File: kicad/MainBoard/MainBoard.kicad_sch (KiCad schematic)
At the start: 97 parts, among them J1 CHAN1, J10 ACC Port, J11 433TX, J12 VDC INPUT, J13 BAT, J14 TRG1, J15 TRG2, J16 FP-BUTTONS, J17 EXPAN2, J18 OUTPUT_BOARD_POWER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

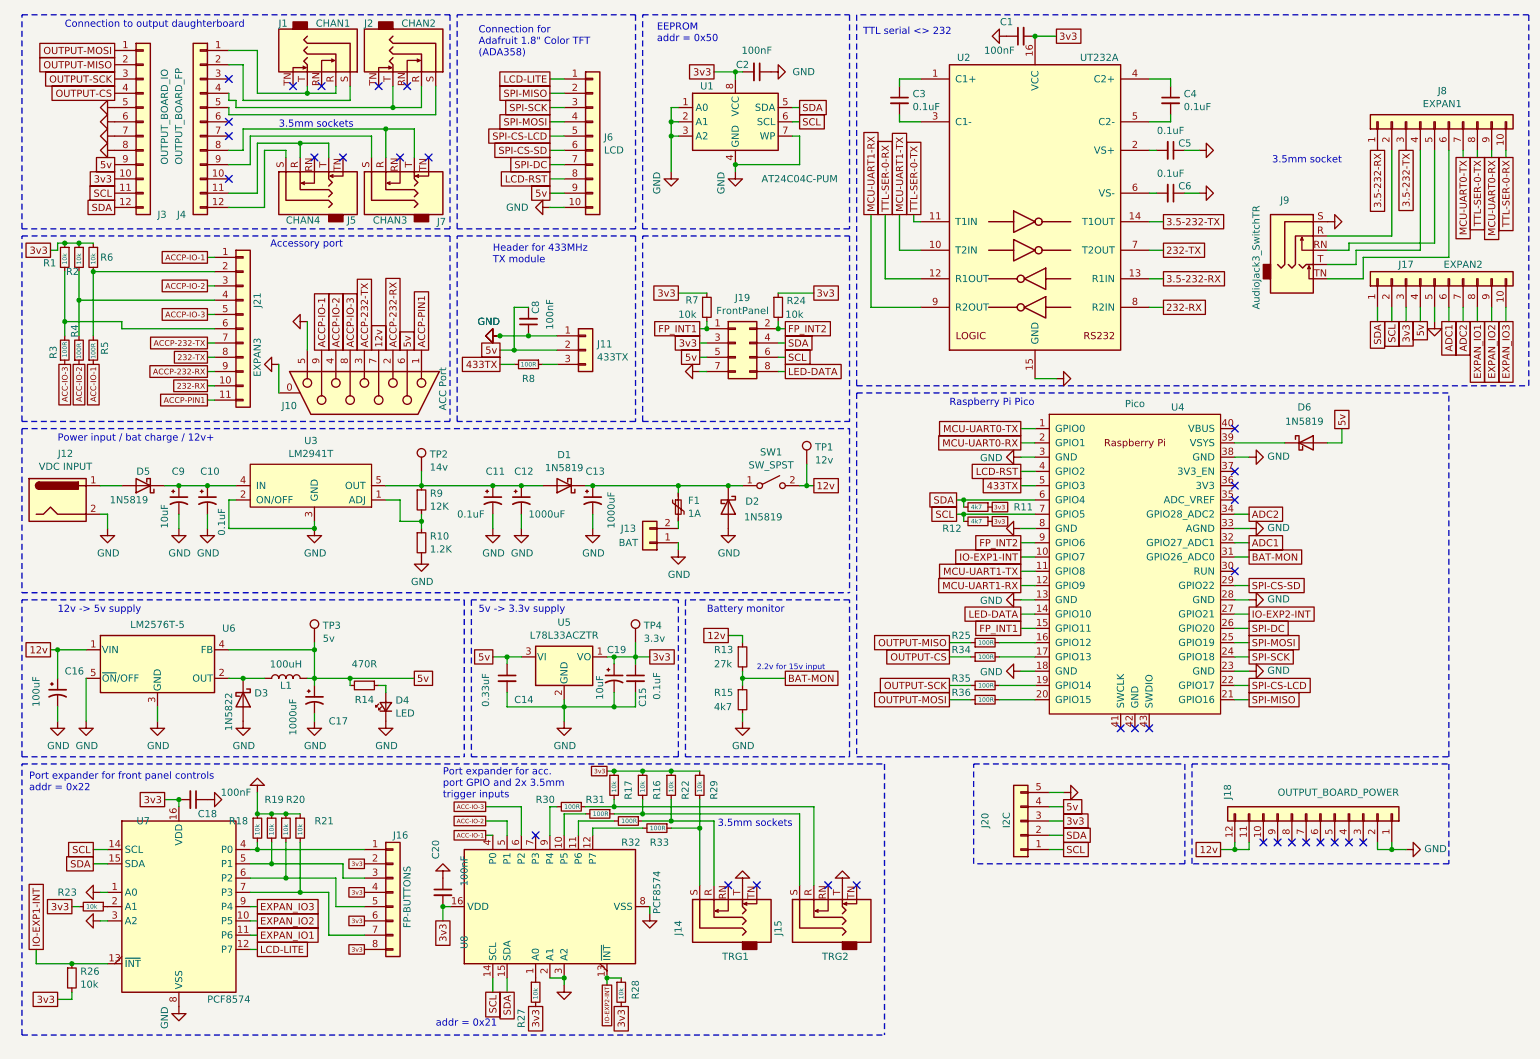
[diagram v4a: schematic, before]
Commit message: No more 12v rs232 - move to UART
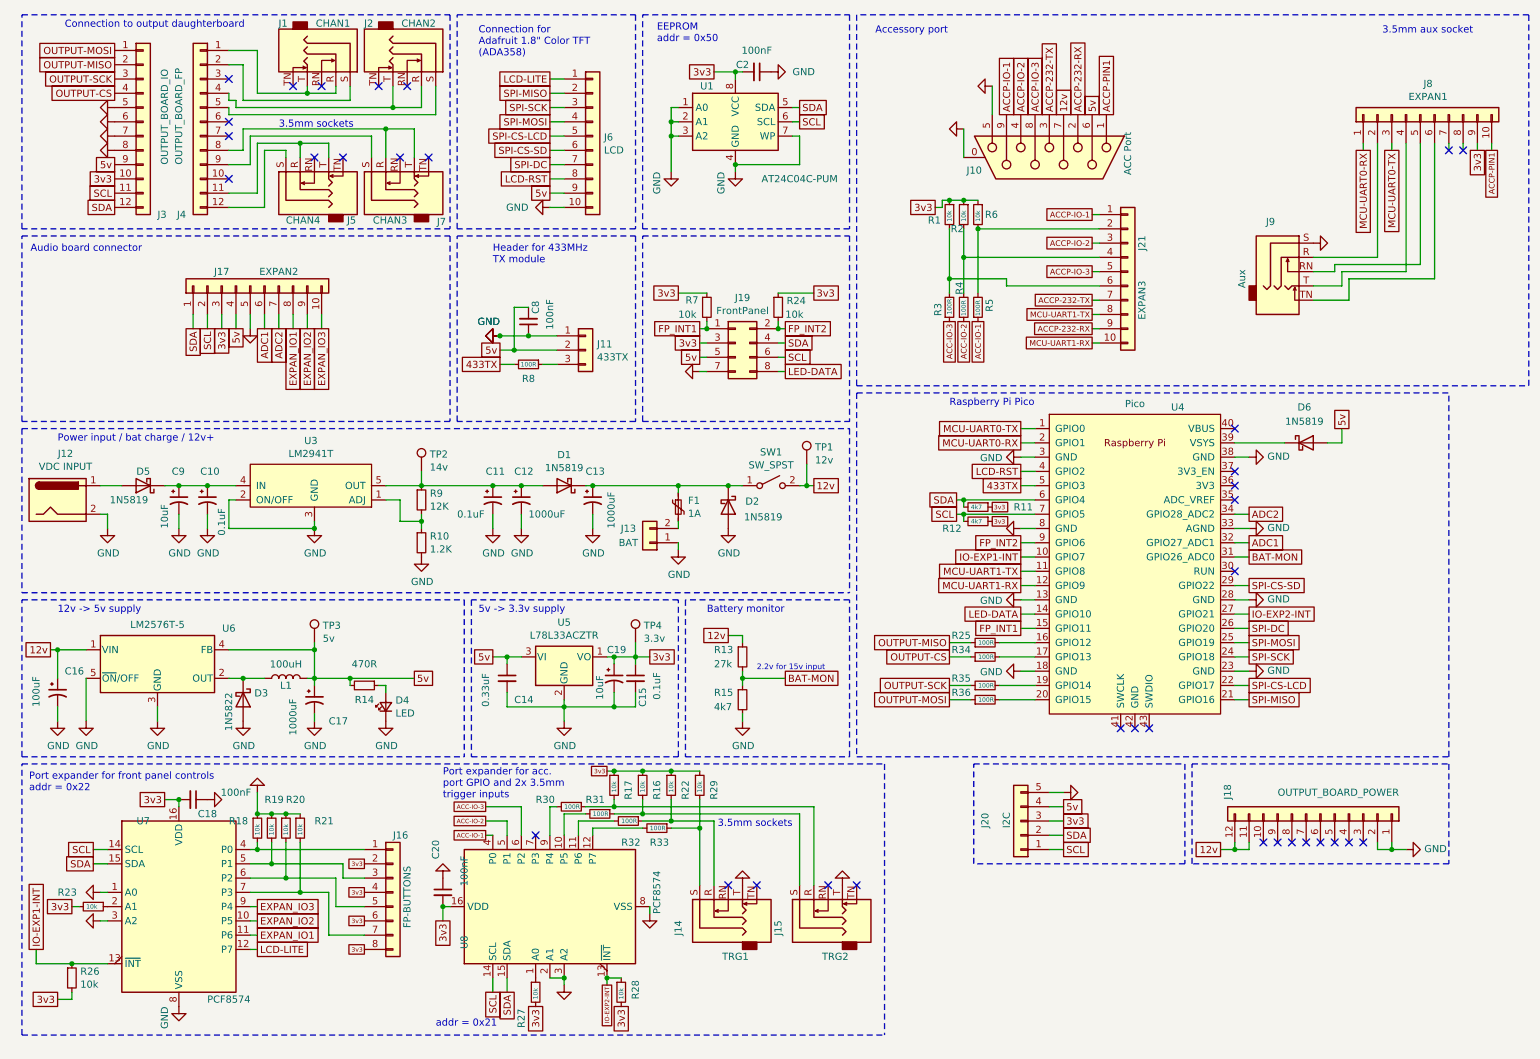
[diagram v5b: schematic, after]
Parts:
- removed C1: 100nF, Capacitor_THT:C_Disc_D3.0mm_W2.0mm_P2.50mm, symbol Device:C_Small
- removed C3, C4, C5, C6: 0.1uF, Capacitor_THT:C_Disc_D3.0mm_W2.0mm_P2.50mm, symbol Device:C_Small
- removed J21: EXPAN3, Connector_PinSocket_2.54mm:PinSocket_1x11_P2.54mm_Vertical, symbol Connector_Generic:Conn_01x11
- removed U2: UT232A, Package_DIP:DIP-16_W7.62mm_Socket, symbol Interface_UART:MAX232
- added J21: EXPAN3, Connector_PinSocket_2.54mm:PinSocket_1x10_P2.54mm_Vertical, symbol Connector_Generic:Conn_01x10
- J9: value AudioJack3_SwitchTR -> Aux
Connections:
- net 3.5-232-RX is gone; now on net MCU-UART0-RX: J8.1 (Pin_1)
- net 3.5-232-TX is gone; now on net MCU-UART0-TX: J8.3 (Pin_3)
- net TTL-SER-0-RX is gone; now on net ACCP-PIN1: J8.10 (Pin_10)
- net 3v3: now also J8.9 (Pin_9)
- net ACCP-232-RX: now also J21.9 (Pin_9)
- net ACCP-232-TX: now also J21.7 (Pin_7)
- net ACCP-IO-1: now also J21.1 (Pin_1)
- net ACCP-IO-2: now also J21.3 (Pin_3)
- net ACCP-IO-3: now also J21.5 (Pin_5)
- net MCU-UART0-RX: no longer J8.9 (Pin_9)
- net MCU-UART0-TX: no longer J8.7 (Pin_7)
- net MCU-UART1-RX: now also J21.10 (Pin_10)
- net MCU-UART1-TX: now also J21.8 (Pin_8)
- net at R5.2, R6.2: now also J21.2 (Pin_2)
- net at R2.2, R4.2: now also J21.4 (Pin_4)
- net at R1.2, R3.2: now also J21.6 (Pin_6)
- net TTL-SER-0-TX: no longer names the net of J8.8 (Pin_8)
- no-connect marks 33 -> 35
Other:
- note added: "3.5mm aux socket"
- note added: "Audio board connector"
- note removed: "3.5mm socket"
- note removed: "TTL serial <> 232"
- moved on the sheet: J10, J17, J8, J9, R1, R2, R3, R4, R5, R6

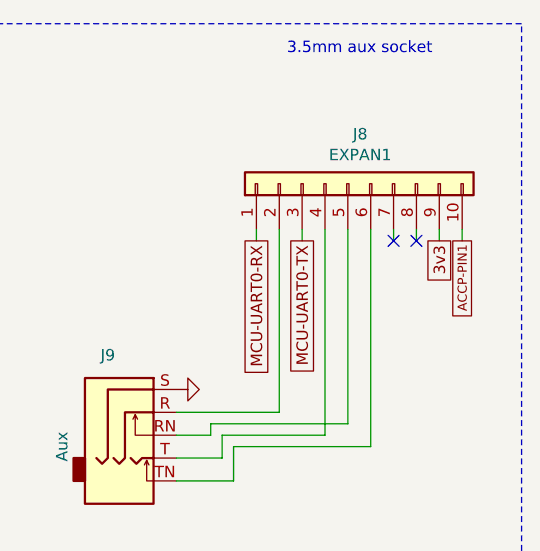
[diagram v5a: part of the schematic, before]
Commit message: Small changes to expander
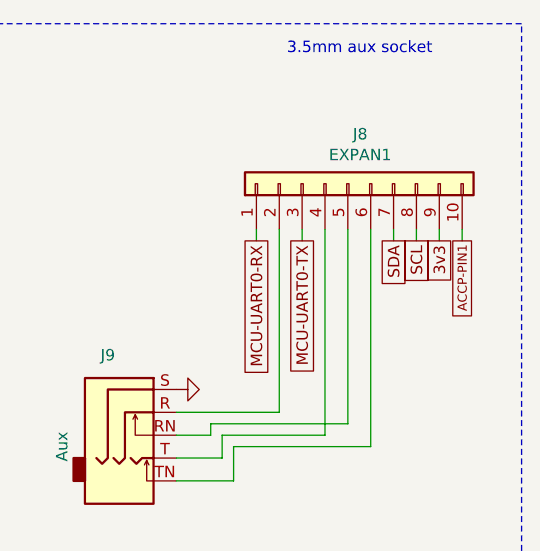
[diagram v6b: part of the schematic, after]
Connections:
- net SCL: now also J8.8 (Pin_8)
- net SDA: now also J8.7 (Pin_7)
- no-connect marks 35 -> 33
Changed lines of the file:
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@@
 	)
 	(no_connect
-		(at 271.78 38.1)
-	)
-	(no_connect
 		(at 231.14 113.03)
 	)
@@
 	)
 	(no_connect
-		(at 269.24 38.1)
-	)
-	(no_connect
 		(at 72.39 39.37)
 	)
@@
 		)
 	)
-	(wire
-		(pts
-			(xy 269.24 38.1) (xy 269.24 36.83)
-		)
-		(stroke
-			(width 0)
-			(type default)
-		)
-	)
 	(polyline
 		(pts
@@
 	(wire
 		(pts
+			(xy 271.78 38.1) (xy 271.78 36.83)
+		)
+		(stroke
+			(width 0)
+			(type default)
+		)
+	)
+	(wire
+		(pts
 			(xy 180.34 46.99) (xy 182.88 46.99)
 		)
@@
 	(wire
 		(pts
-			(xy 271.78 36.83) (xy 271.78 38.1)
-		)
-		(stroke
-			(width 0)
-			(type default)
-		)
-	)
-	(wire
-		(pts
 			(xy 24.13 182.88) (xy 30.48 182.88)
 		)
@@
 	(wire
 		(pts
+			(xy 269.24 38.1) (xy 269.24 36.83)
+		)
+		(stroke
+			(width 0)
+			(type default)
+		)
+	)
+	(wire
+		(pts
 			(xy 71.12 167.64) (xy 71.12 172.72)
 		)
@@
 		)
 	)
+	(global_label "SDA"
+		(shape passive)
+		(at 269.24 38.1 270)
+		(effects
+			(font
+				(size 1.27 1.27)
+			)
+			(justify right)
+		)
+		(property "Intersheetrefs" "${INTERSHEET_REFS}"
+			(at 269.24 38.1 0)
+			(effects
+				(font
+					(size 1.27 1.27)
+				)
+				(hide yes)
+			)
+		)
+	)
 	(global_label "EXPAN_IO3"
 		(shape passive)
@@
 			(effects
 				(font
+					(size 1.27 1.27)
+				)
+				(hide yes)
+			)
+		)
+	)
+	(global_label "SCL"
+		(shape passive)
+		(at 271.78 38.1 270)
+		(effects
+			(font
+				(size 1.27 1.27)
+			)
+			(justify right)
+		)
+		(property "Intersheetrefs" "${INTERSHEET_REFS}"
+			(at 271.78 38.1 0)
+			(effects
+				(font

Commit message: Fix connections of output jacks
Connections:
- net at J1.T, J4.1 (Pin_1): no longer J1.R
- net at J4.11 (Pin_11), J5.T: no longer J5.R
- net at J2.T, J4.4 (Pin_4): no longer J2.R
- net at J4.8 (Pin_8), J7.T: no longer J7.R
- no-connect marks 33 -> 37
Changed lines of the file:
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@@
 	)
 	(junction
-		(at 66.04 27.94)
-		(diameter 0)
-		(color 0 0 0 0)
-	)
-	(junction
 		(at 86.36 104.14)
 		(diameter 0)
@@
 	)
 	(junction
-		(at 64.77 36.83)
-		(diameter 0)
-		(color 0 0 0 0)
-	)
-	(junction
 		(at 86.36 97.79)
 		(diameter 0)
@@
 	)
 	(junction
-		(at 81.28 30.48)
-		(diameter 0)
-		(color 0 0 0 0)
-	)
-	(junction
 		(at 62.23 167.64)
 		(diameter 0)
@@
 	)
 	(junction
-		(at 80.01 34.29)
-		(diameter 0)
-		(color 0 0 0 0)
-	)
-	(junction
 		(at 130.81 33.02)
 		(diameter 0)
@@
 	)
 	(no_connect
+		(at 64.77 39.37)
+	)
+	(no_connect
 		(at 231.14 100.33)
 	)
@@
 	)
 	(no_connect
+		(at 80.01 39.37)
+	)
+	(no_connect
 		(at 52.07 25.4)
 	)
 	(no_connect
+		(at 86.36 26.67)
+	)
+	(no_connect
 		(at 52.07 43.18)
 	)
@@
 	)
 	(no_connect
+		(at 71.12 26.67)
+	)
+	(no_connect
 		(at 231.14 95.25)
 	)
@@
 	(wire
 		(pts
-			(xy 80.01 34.29) (xy 85.09 34.29)
-		)
-		(stroke
-			(width 0)
-			(type default)
-		)
-	)
-	(wire
-		(pts
 			(xy 66.04 27.94) (xy 66.04 26.67)
 		)
@@
 	(wire
 		(pts
+			(xy 52.07 31.75) (xy 88.9 31.75)
+		)
+		(stroke
+			(width 0)
+			(type default)
+		)
+	)
+	(wire
+		(pts
 			(xy 20.32 127) (xy 21.59 127)
 		)
@@
 	(wire
 		(pts
-			(xy 80.01 34.29) (xy 80.01 39.37)
-		)
-		(stroke
-			(width 0)
-			(type default)
-		)
-	)
-	(wire
-		(pts
 			(xy 264.16 36.83) (xy 264.16 58.42)
 		)
@@
 		)
 	)
-	(wire
-		(pts
-			(xy 66.04 27.94) (xy 71.12 27.94)
-		)
-		(stroke
-			(width 0)
-			(type default)
-		)
-	)
 	(polyline
 		(pts
@@
 	(wire
 		(pts
-			(xy 86.36 30.48) (xy 86.36 26.67)
-		)
-		(stroke
-			(width 0)
-			(type default)
-		)
-	)
-	(wire
-		(pts
 			(xy 245.11 59.69) (xy 248.92 59.69)
 		)
@@
 	(wire
 		(pts
-			(xy 81.28 30.48) (xy 86.36 30.48)
-		)
-		(stroke
-			(width 0)
-			(type default)
-		)
-	)
-	(wire
-		(pts
 			(xy 124.46 128.27) (xy 127 128.27)
 		)
@@
 	(wire
 		(pts
-			(xy 57.15 36.83) (xy 64.77 36.83)
+			(xy 57.15 36.83) (xy 69.85 36.83)
 		)
 		(stroke
@@
 	(wire
 		(pts
-			(xy 71.12 27.94) (xy 71.12 26.67)
-		)
-		(stroke
-			(width 0)
-			(type default)
-		)
-	)
-	(wire
-		(pts
 			(xy 271.78 38.1) (xy 271.78 36.83)
 		)
@@
 	(wire
 		(pts
-			(xy 64.77 36.83) (xy 69.85 36.83)
-		)
-		(stroke
-			(width 0)
-			(type default)
-		)
-	)
-	(wire
-		(pts
 			(xy 102.87 73.66) (xy 110.49 73.66)
 		)
@@
 	(wire
 		(pts
-			(xy 52.07 31.75) (xy 88.9 31.75)
-		)
-		(stroke
-			(width 0)
-			(type default)
-		)
-	)
-	(wire
-		(pts
-			(xy 54.61 34.29) (xy 80.01 34.29)
+			(xy 54.61 34.29) (xy 85.09 34.29)
 		)
 		(stroke
@@
 		)
 		(stroke
-			(width 0)
-			(type default)
-		)
-	)
-	(wire
-		(pts
-			(xy 64.77 36.83) (xy 64.77 39.37)
-		)
-		(stroke
